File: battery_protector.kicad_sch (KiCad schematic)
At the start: 14 parts, among them J1 Screw_Terminal_01x02, J2 Screw_Terminal_01x02

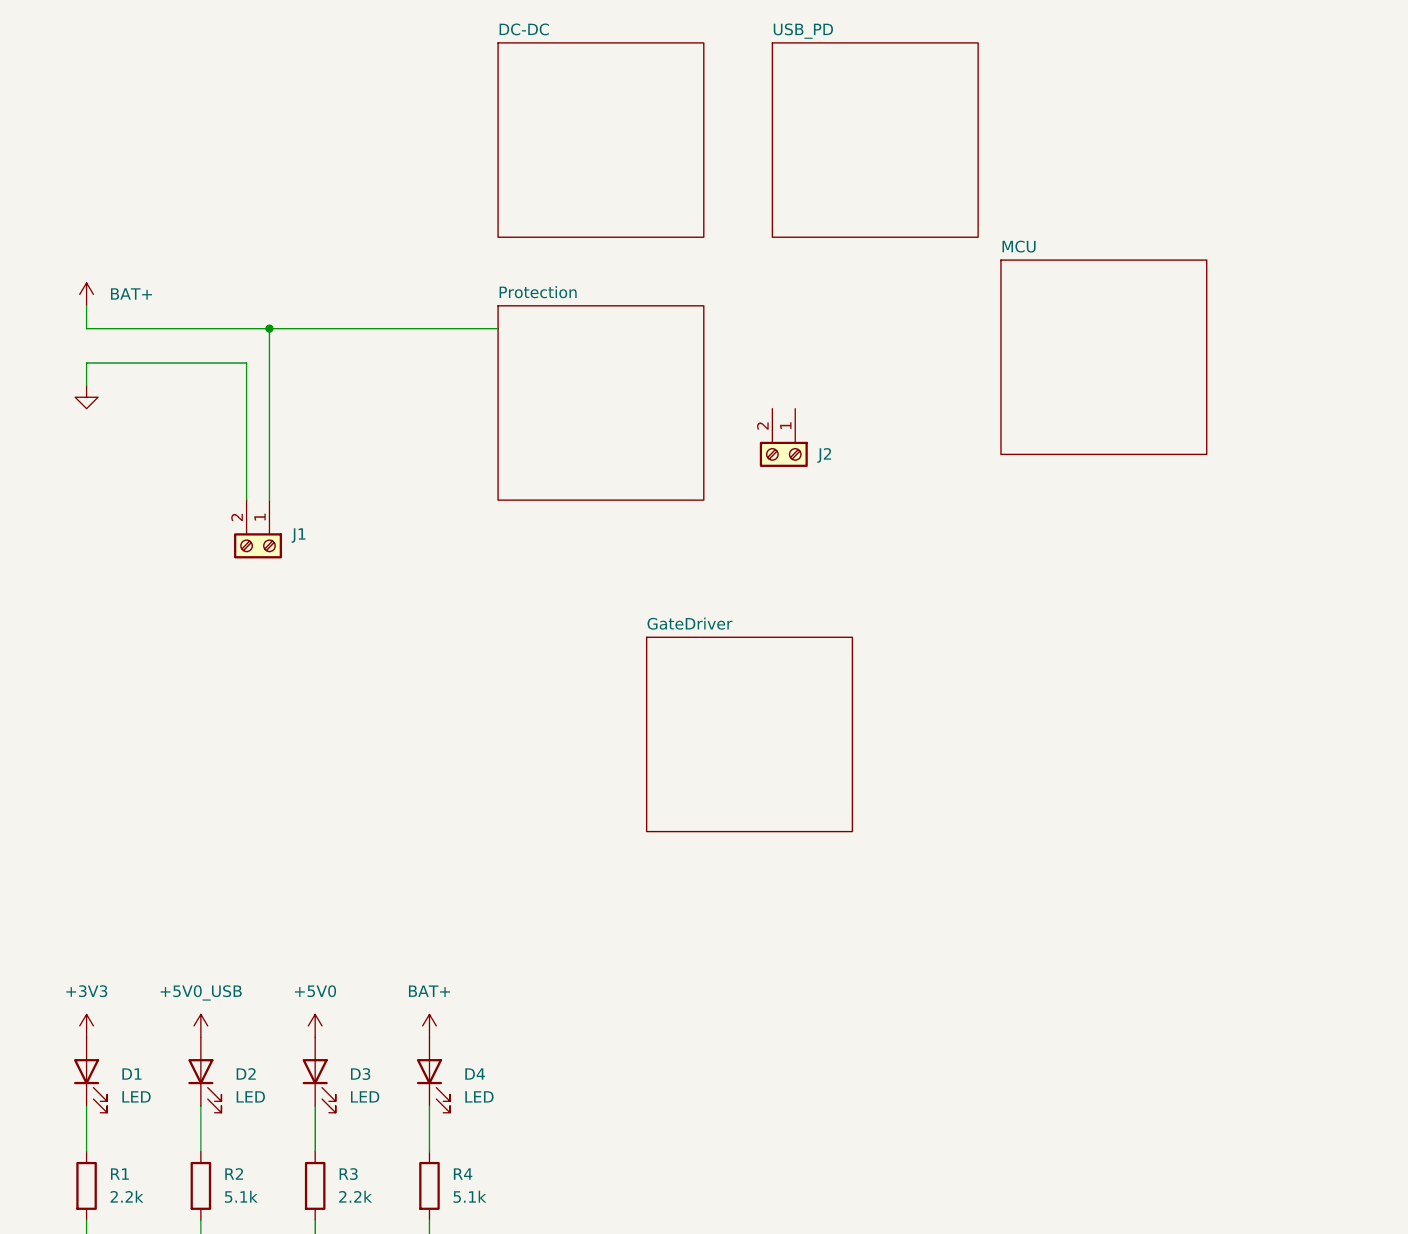
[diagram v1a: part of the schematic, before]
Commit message: finish protection sheet
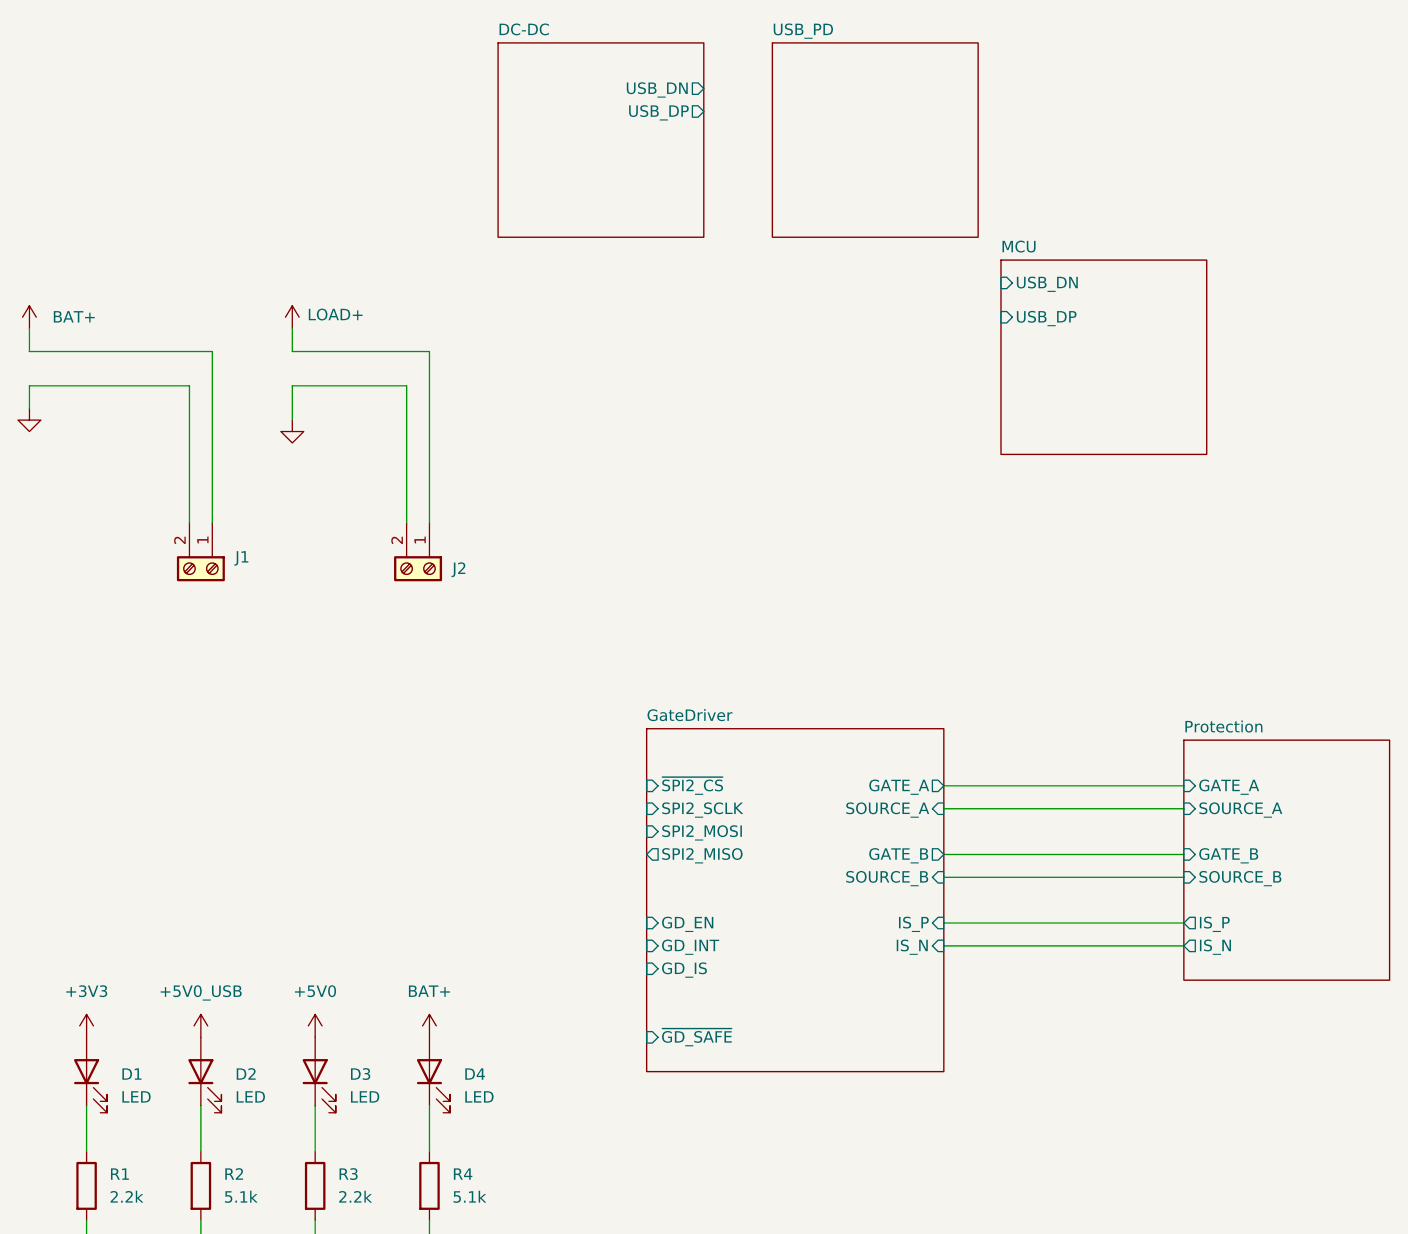
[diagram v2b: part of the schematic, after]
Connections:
- net GND: now also J2.2 (Pin_2)
- net LOAD+: now reaches J2.1 (Pin_1)
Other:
- sheet DC-DC ports: added USB_DN, USB_DP; removed none
- sheet GateDriver ports: added GATE_A, GATE_B, GD_EN, GD_INT, GD_IS, IS_N, IS_P, SOURCE_A, SOURCE_B, SPI2_MISO, SPI2_MOSI, SPI2_SCLK, ~{GD_SAFE}, ~{SPI2_CS}; removed none
- sheet MCU ports: added USB_DN, USB_DP; removed none
- sheet Protection ports: added GATE_A, GATE_B, IS_N, IS_P, SOURCE_A, SOURCE_B; removed none
- moved on the sheet: J1, J2

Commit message: Added footprints to resistors and capacitors, and fixed the mosfets wiring issue (#4)
Jul9th push. Added footprints to resistors and capacitors, and fixed the mosfets wiring issue
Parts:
- R1, R2, R3, R4: footprint (none) -> Resistor_SMD:R_0603_1608Metric
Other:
- removed sheet USB_PD
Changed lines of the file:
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@@
 			)
 		)
-		(property "Footprint" ""
+		(property "Footprint" "Resistor_SMD:R_0603_1608Metric"
 			(at 49.022 177.8 90)
 			(effects
@@
 			)
 		)
-		(property "Footprint" ""
+		(property "Footprint" "Resistor_SMD:R_0603_1608Metric"
 			(at 23.622 177.8 90)
 			(effects
@@
 			)
 		)
-		(property "Footprint" ""
+		(property "Footprint" "Resistor_SMD:R_0603_1608Metric"
 			(at 36.322 177.8 90)
 			(effects
@@
 			)
 		)
-		(property "Footprint" ""
+		(property "Footprint" "Resistor_SMD:R_0603_1608Metric"
 			(at 61.722 177.8 90)
 			(effects
@@
 				)
 			)
-		)
-	)
-	(sheet
-		(at 101.6 50.8)
-		(size 22.86 21.59)
-		(exclude_from_sim no)
-		(in_bom yes)
-		(on_board yes)
-		(dnp no)
-		(fields_autoplaced yes)
-		(stroke
-			(width 0.1524)
-			(type solid)
-		)
-		(fill
-			(color 0 0 0 0.0000)
-		)
-		(property "Sheetname" "USB_PD"
-			(at 101.6 50.0884 0)
-			(effects
-				(font
-					(size 1.27 1.27)
-				)
-				(justify left bottom)
-			)
-		)
-		(property "Sheetfile" "USB_PD.kicad_sch"
-			(at 101.6 72.9746 0)
-			(effects
-				(font
-					(size 1.27 1.27)
-				)
-				(justify left top)
-				(hide yes)
-			)
-		)
-		(instances
-			(project "battery_protector"
-				(path "/b2975477-3b95-446c-b662-4cca32764c73"
-					(page "6")
-				)
-			)

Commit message: finish schematic
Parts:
- D1, D2, D3, D4: footprint (none) -> LED_SMD:LED_0603_1608Metric
- H1, H2, H3, H4: footprint (none) -> MountingHole:MountingHole_3.2mm_M3_Pad_TopBottom
- J1, J2: value Screw_Terminal_01x02 -> TB005-762-02BE; footprint (none) -> custom_footprints:CUI_TB005-762-02BE
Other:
- sheet MCU ports: added GD_EN, GD_INT, GD_IS, SPI2_MISO, SPI2_MOSI, SPI2_SCLK, ~{GD_SAFE}, ~{SPI2_CS}; removed none
- moved on the sheet: J2

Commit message: setup layout rules
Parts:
- removed H1, H2, H3, H4: MH1, MountingHole:MountingHole_3.2mm_M3_Pad_TopBottom, symbol Mechanical:MountingHole_Pad_MP
- added H5, H6, H7, H8: MountingHole_Pad, MountingHole:MountingHole_3.2mm_M3_Pad_TopBottom, symbol Mechanical:MountingHole_Pad
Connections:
- net GND: now also H5.1, H6.1, H7.1, H8.1
- no-connect marks 1 -> 0

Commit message: Did some more routing
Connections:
- net +5V0 renamed +5V0_board
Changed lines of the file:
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@@
 		(on_board yes)
 		(dnp no)
-		(fields_autoplaced yes)
 		(property "Reference" "#PWR0110"
 			(at 50.8 165.1 0)
@@
 			)
 		)
-		(property "Value" "+5V0"
+		(property "Value" "+5V0_board"
 			(at 50.8 156.21 0)
 			(effects
@@
 	)
 	(symbol
+		(lib_id "power:PWR_FLAG")
+		(at 25.4 240.03 180)
+		(unit 1)
+		(exclude_from_sim no)
+		(in_bom yes)
+		(on_board yes)
+		(dnp no)
+		(fields_autoplaced yes)
+		(property "Reference" "#FLG01"
+			(at 25.4 241.935 0)
+			(effects
+				(font
+					(size 1.27 1.27)
+				)
+				(hide yes)
+			)
+		)
+		(property "Value" "PWR_FLAG"
+			(at 25.4 245.11 0)
+			(effects
+				(font
+					(size 1.27 1.27)
+				)
+			)
+		)
+		(property "Footprint" ""
+			(at 25.4 240.03 0)
+			(effects
+				(font
+					(size 1.27 1.27)
+				)
+				(hide yes)
+			)
+		)
+		(property "Datasheet" "~"
+			(at 25.4 240.03 0)
+			(effects
+				(font
+					(size 1.27 1.27)
+				)
+				(hide yes)
+			)
+		)
+		(property "Description" "Special symbol for telling ERC where power comes from"
+			(at 25.4 240.03 0)
+			(effects
+				(font
+					(size 1.27 1.27)
+				)
+				(hide yes)
+			)
+		)
+		(pin "1"
+		)
+		(instances
+			(project "battery_protector"
+				(path "/b2975477-3b95-446c-b662-4cca32764c73"
+					(reference "#FLG01")
+					(unit 1)
+				)
+			)
+		)
+	)
+	(symbol
 		(lib_id "Mechanical:MountingHole_Pad")
 		(at 63.5 207.01 0)
@@
 					(unit 1)
 				)
+			)
+		)
+	)
+	(symbol
+		(lib_id "power:+5V")
+		(at 25.4 240.03 0)
+		(unit 1)
+		(exclude_from_sim no)
+		(in_bom yes)
+		(on_board yes)
+		(dnp no)
+		(fields_autoplaced yes)
+		(property "Reference" "#PWR02"
+			(at 25.4 243.84 0)
+			(effects
+				(font
+					(size 1.27 1.27)
+				)
+				(hide yes)
+			)
+		)
+		(property "Value" "+5V0_board"
+			(at 25.4 234.95 0)
+			(effects
+				(font
+					(size 1.27 1.27)
+				)
+			)
+		)
+		(property "Footprint" ""
+			(at 25.4 240.03 0)
+			(effects
+				(font
+					(size 1.27 1.27)
+				)
+				(hide yes)
+			)
+		)
+		(property "Datasheet" ""
+			(at 25.4 240.03 0)
+			(effects
+				(font
+					(size 1.27 1.27)
+				)
+				(hide yes)
+			)
+		)
+		(property "Description" "Power symbol creates a global label with name \"+5V\""
+			(at 25.4 240.03 0)
+			(effects
+				(font
+					(size 1.27 1.27)
+				)
+				(hide yes)
+			)
+		)
+		(pin "1"
+		)
+		(instances
+			(project "battery_protector"
+				(path "/b2975477-3b95-446c-b662-4cca32764c73"
+					(reference "#PWR02")
+					(unit 1)
+				)

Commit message: add manufacturer, mpn, and package to bom
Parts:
- D1, D2, D3, D4: Manufacturer_Name (none) -> Lite-On Inc.; Manufacturer_Part_Number (none) -> LTST-C190GKT; Package (none) -> 603
- J1, J2: Manufacturer_Name (none) -> Same Sky (Formerly CUI Devices); Manufacturer_Part_Number (none) -> TB005-762-02BE; Package (none) -> 2POS
- R1, R3: Manufacturer_Name (none) -> YAGEO; Manufacturer_Part_Number (none) -> RC0603FR-072K2L; Package (none) -> 603
- R2, R4: Manufacturer_Name (none) -> YAGEO; Manufacturer_Part_Number (none) -> RC0603FR-075K1L; Package (none) -> 603

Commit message: Caught some issues and made final changes for manufacturing (#9)
Caught some issues and made final changes for manufacturing including correcting the imu and J2 footprints, updating the clearance rules we imported from pcbway (.09mm->0.1mm), and the addition of stitching capacitors for usb signal.
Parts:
- H5, H6, H7, H8: now not fitted
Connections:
- net GND: now also J2.1 (Pin_1); no longer J2.2 (Pin_2)
- net LOAD+: now also J2.2 (Pin_2); no longer J2.1 (Pin_1)
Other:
- moved on the sheet: J2
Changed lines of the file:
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@@
-	(wire
-		(pts
-			(xy 48.26 85.09) (xy 67.31 85.09)
-		)
-		(stroke
-			(width 0)
-			(type default)
-		)
-	)
 	(wire
 		(pts
@@
 	(wire
 		(pts
+			(xy 66.04 85.09) (xy 46.99 85.09)
+		)
+		(stroke
+			(width 0)
+			(type default)
+		)
+	)
+	(wire
+		(pts
 			(xy 25.4 181.61) (xy 25.4 190.5)
 		)
@@
 	(wire
 		(pts
-			(xy 48.26 85.09) (xy 48.26 82.55)
+			(xy 49.53 88.9) (xy 49.53 104.14)
 		)
 		(stroke
@@
 	(wire
 		(pts
+			(xy 66.04 88.9) (xy 49.53 88.9)
+		)
+		(stroke
+			(width 0)
+			(type default)
+		)
+	)
+	(wire
+		(pts
 			(xy 149.86 81.28) (xy 158.75 81.28)
 		)
@@
 	(wire
 		(pts
+			(xy 66.04 88.9) (xy 66.04 92.71)
+		)
+		(stroke
+			(width 0)
+			(type default)
+		)
+	)
+	(wire
+		(pts
 			(xy 19.05 88.9) (xy 36.83 88.9)
 		)
@@
 	(wire
 		(pts
+			(xy 46.99 85.09) (xy 46.99 104.14)
+		)
+		(stroke
+			(width 0)
+			(type default)
+		)
+	)
+	(wire
+		(pts
 			(xy 111.76 88.9) (xy 127 88.9)
 		)
@@
 	(wire
 		(pts
-			(xy 67.31 85.09) (xy 67.31 104.14)
-		)
-		(stroke
-			(width 0)
-			(type default)
-		)
-	)
-	(wire
-		(pts
-			(xy 48.26 88.9) (xy 64.77 88.9)
-		)
-		(stroke
-			(width 0)
-			(type default)
-		)
-	)
-	(wire
-		(pts
 			(xy 149.86 91.44) (xy 207.01 91.44)
 		)
@@
 	(wire
 		(pts
-			(xy 64.77 88.9) (xy 64.77 104.14)
-		)
-		(stroke
-			(width 0)
-			(type default)
-		)
-	)
-	(wire
-		(pts
 			(xy 198.12 81.28) (xy 207.01 81.28)
 		)
@@
 	(wire
 		(pts
-			(xy 48.26 88.9) (xy 48.26 92.71)
+			(xy 66.04 85.09) (xy 66.04 82.55)
 		)
 		(stroke
@@
 		(in_bom no)
 		(on_board yes)
-		(dnp no)
+		(dnp yes)
 		(fields_autoplaced yes)
 		(property "Reference" "H5"
@@
 	(symbol
 		(lib_id "Connector:Screw_Terminal_01x02")
-		(at 67.31 109.22 270)
+		(at 49.53 109.22 270)
 		(unit 1)
 		(exclude_from_sim no)
@@
 		(dnp no)
 		(property "Reference" "J2"
-			(at 69.85 108.204 90)
+			(at 45.466 112.5221 90)
 			(effects
 				(font
@@
 		)
 		(property "Value" "TB005-762-02BE"
-			(at 69.85 110.4899 90)
+			(at 45.466 114.808 90)
 			(effects
 				(font
@@
 				)
 				(justify left)
+				(hide yes)
 			)
 		)
 		(property "Footprint" "custom_footprints:CUI_TB005-762-02BE"
-			(at 67.31 109.22 0)
+			(at 49.53 109.22 0)
 			(effects
 				(font
@@
 		)
 		(property "Datasheet" "https://www.sameskydevices.com/product/resource/tb005-762.pdf"
-			(at 67.31 109.22 0)
+			(at 49.53 109.22 0)
 			(effects
 				(font
@@
 		)
 		(property "Description" "Generic screw terminal, single row, 01x02, script generated (kicad-library-utils/schlib/autogen/connector/)"
-			(at 67.31 109.22 0)
+			(at 49.53 109.22 0)
 			(effects
 				(font
@@
 		)
 		(property "Manufacturer_Name" "Same Sky (Formerly CUI Devices)"
-			(at 67.31 109.22 0)
+			(at 49.53 109.22 0)
 			(effects
 				(font
@@
 		)
 		(property "Manufacturer_Part_Number" "TB005-762-02BE"
-			(at 67.31 109.22 0)
+			(at 49.53 109.22 0)
 			(effects
 				(font
@@
 		)
 		(property "Package" "2POS"
-			(at 67.31 109.22 0)
+			(at 49.53 109.22 0)
 			(effects
 				(font
@@
 	(symbol
 		(lib_id "power:GND")
-		(at 48.26 92.71 0)
+		(at 66.04 92.71 0)
+		(mirror y)
 		(unit 1)
 		(exclude_from_sim no)
@@
 		(fields_autoplaced yes)
 		(property "Reference" "#PWR0115"
-			(at 48.26 99.06 0)
+			(at 66.04 99.06 0)
 			(effects
 				(font
@@
 		)
 		(property "Value" "GND"
-			(at 48.26 97.79 0)
+			(at 66.04 97.79 0)
 			(effects
 				(font
@@
 		)
 		(property "Footprint" ""
-			(at 48.26 92.71 0)
+			(at 66.04 92.71 0)
 			(effects
 				(font
@@
 		)
 		(property "Datasheet" ""
-			(at 48.26 92.71 0)
+			(at 66.04 92.71 0)
 			(effects
 				(font
@@
 		)
 		(property "Description" "Power symbol creates a global label with name \"GND\" , ground"
-			(at 48.26 92.71 0)
+			(at 66.04 92.71 0)
 			(effects
 				(font
@@
 		(on_board yes)
 		(dnp no)
-		(fields_autoplaced yes)
 		(property "Reference" "J1"
-			(at 41.91 107.9499 90)
+			(at 35.306 112.268 90)
 			(effects
 				(font
@@
 		)
 		(property "Value" "TB005-762-02BE"
-			(at 41.91 110.4899 90)
+			(at 35.306 114.808 90)
 			(effects
 				(font
@@
 				)
 				(justify left)
+				(hide yes)
 			)
 		)
@@
 	(symbol
 		(lib_id "power:+3V3")
-		(at 48.26 82.55 0)
+		(at 66.04 82.55 0)
+		(mirror y)
 		(unit 1)
 		(exclude_from_sim no)
@@
 		(dnp no)
 		(property "Reference" "#PWR0114"
-			(at 48.26 86.36 0)
+			(at 66.04 86.36 0)
 			(effects
 				(font
@@
 		)
 		(property "Value" "LOAD+"
-			(at 53.086 81.026 0)
+			(at 61.214 81.026 0)
 			(effects
 				(font
@@
 		)
 		(property "Footprint" ""
-			(at 48.26 82.55 0)
+			(at 66.04 82.55 0)
 			(effects
 				(font
@@
 		)
 		(property "Datasheet" ""
-			(at 48.26 82.55 0)
+			(at 66.04 82.55 0)
 			(effects
 				(font
@@
 		)
 		(property "Description" "Power symbol creates a global label with name \"+3V3\""
-			(at 48.26 82.55 0)
+			(at 66.04 82.55 0)
 			(effects
 				(font
@@
 		(in_bom no)
 		(on_board yes)
-		(dnp no)
+		(dnp yes)
 		(fields_autoplaced yes)
 		(property "Reference" "H6"
@@
 		(in_bom no)
 		(on_board yes)
-		(dnp no)
+		(dnp yes)
 		(fields_autoplaced yes)
 		(property "Reference" "H8"
@@
 		(in_bom no)
 		(on_board yes)
-		(dnp no)
+		(dnp yes)
 		(fields_autoplaced yes)
 		(property "Reference" "H7"
